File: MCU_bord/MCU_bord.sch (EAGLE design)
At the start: 1 part

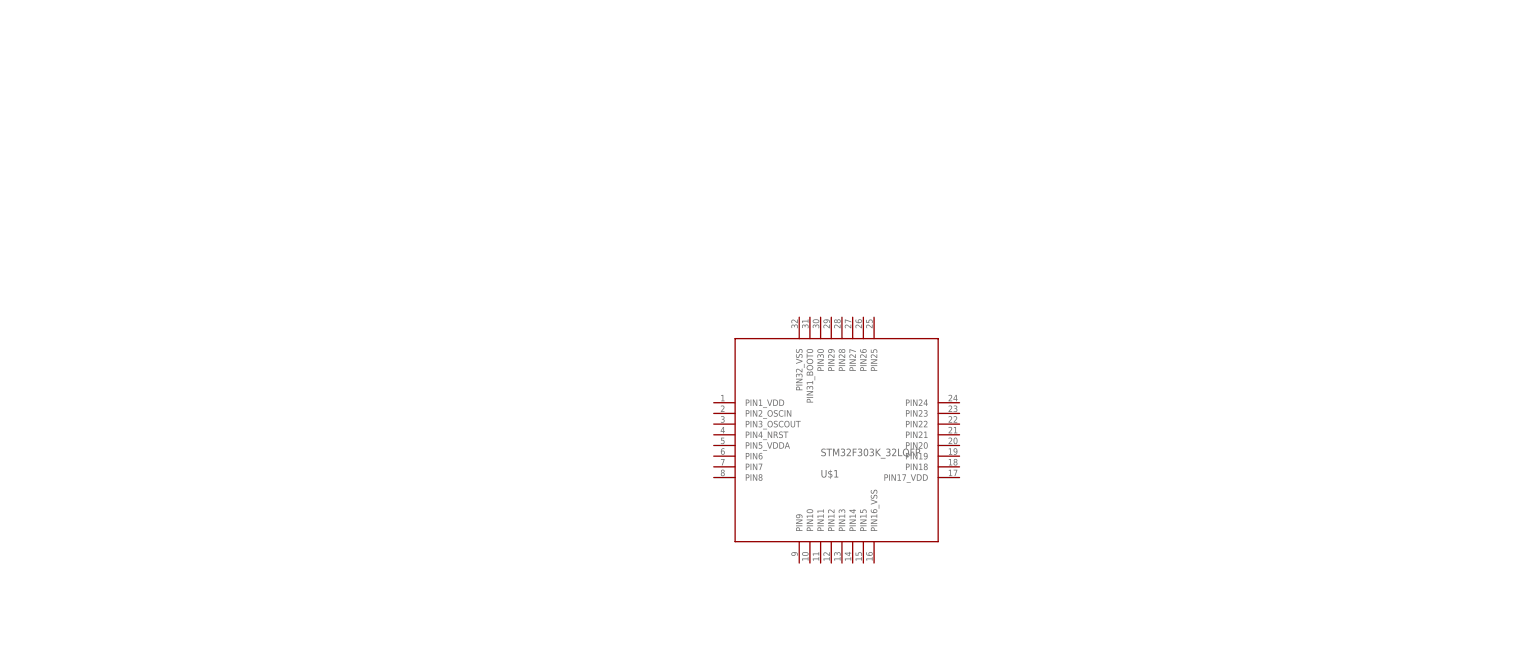
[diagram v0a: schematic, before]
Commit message: mcu側に着手
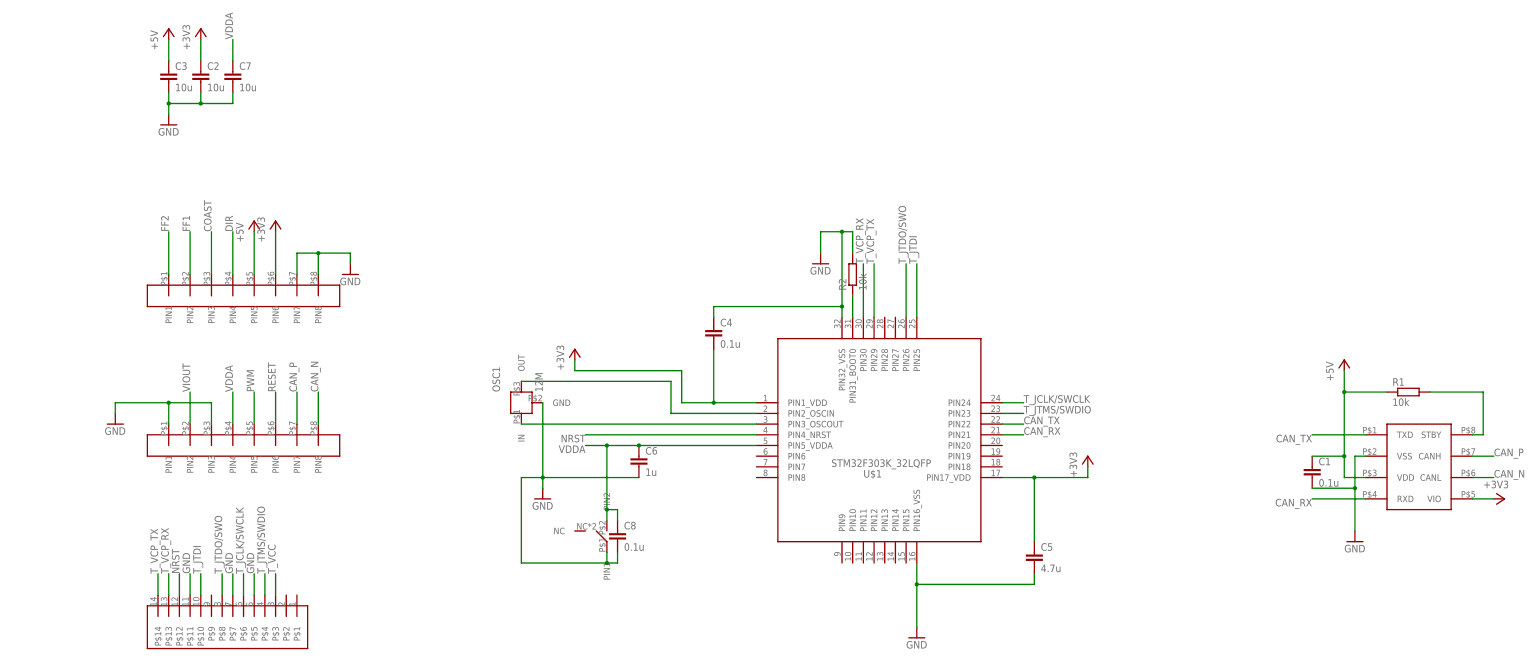
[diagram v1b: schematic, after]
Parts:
- added C1, C4, C8: 0.1u, rcl:C-EUC1608
- added C2, C3, C7: 10u, rcl:C-EUC1608
- added C5: 4.7u, rcl:C-EUC1608
- added C6: 1u, rcl:C-EUC1608
- added CON1, CON2: (no value), user_conector:JQ_S8P
- added IC1: (no value), user_ic:MCP2562MCP2561-SN
- added OSC1: 12M, user_osc:CSTN#
- added R1, R2: 10k, user_rcl:R_REG
- added U$2: TAKUTOSUITTI2, user_swich:TAKUTOSUITTI2
- added U$3: BOX14P, user_conector:BOX14P
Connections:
- new net +3V3: C2.1, C4.2, C5.1, CON1.PIN6, IC1.VIO, U$1.PIN17_VDD, U$1.PIN1_VDD
- new net +5V: C1.1, C3.1, CON1.PIN5, IC1.VDD, R1.1
- new net CAN_N: CON2.PIN8, IC1.CANL
- new net CAN_P: CON2.PIN7, IC1.CANH
- new net CAN_RX: IC1.RXD, U$1.PIN21
- new net CAN_TX: IC1.TXD, U$1.PIN22
- new net COAST: CON1.PIN3
- new net DIR: CON1.PIN4
- new net FF1: CON1.PIN2
- new net FF2: CON1.PIN1
- new net GND: C1.2, C2.2, C3.2, C4.1, C5.2, C6.2, C7.2, C8.2, CON1.PIN7, CON1.PIN8, CON2.PIN1, CON2.PIN3, IC1.VSS, OSC1.GND, R2.2, U$1.PIN16_VSS, U$1.PIN32_VSS, U$2.PIN1, U$3.P$11, U$3.P$5, U$3.P$7
- new net N$1: OSC1.IN, U$1.PIN3_OSCOUT
- new net N$2: OSC1.OUT, U$1.PIN2_OSCIN
- new net N$3: R2.1, U$1.PIN31_BOOT0
- new net N$7: IC1.STBY, R1.2
- new net NRST: U$1.PIN4_NRST, U$3.P$12
- new net PWM: CON2.PIN5
- new net RESET: CON2.PIN6
- new net T_JCLK/SWCLK: U$1.PIN24, U$3.P$6
- new net T_JTDI: U$1.PIN25, U$3.P$10
- new net T_JTDO/SWO: U$1.PIN26, U$3.P$8
- new net T_JTMS/SWDIO: U$1.PIN23, U$3.P$4
- new net T_VCC: U$3.P$3
- new net T_VCP_RX: U$1.PIN30, U$3.P$13
- new net T_VCP_TX: U$1.PIN29, U$3.P$14
- new net VDDA: C6.1, C7.1, C8.1, CON2.PIN4, U$1.PIN5_VDDA, U$2.PIN2
- new net VIOUT: CON2.PIN2
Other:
- moved on the sheet: U$1

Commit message: mcu側回路図多分完成。基板側に着手する予定
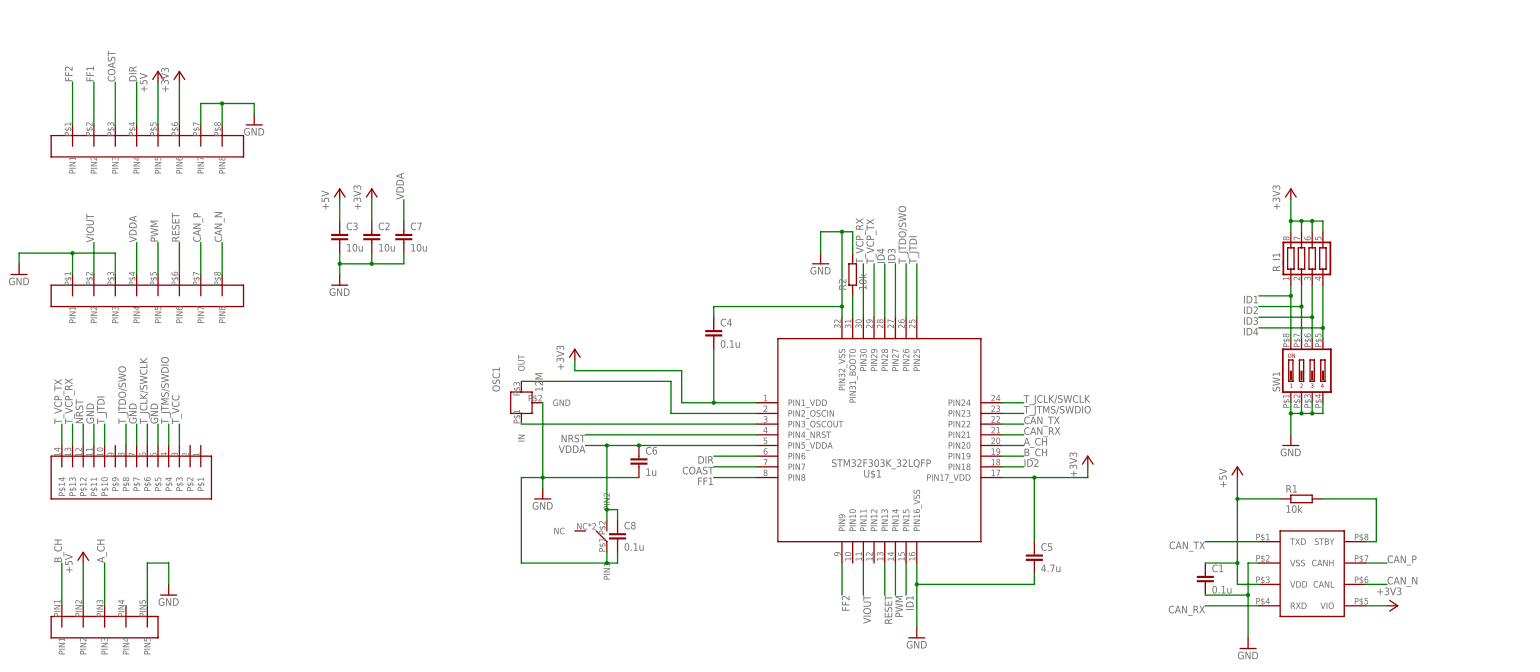
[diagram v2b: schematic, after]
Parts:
- added R_I1: (no value), user_rcl:R_SHUGOU2
- added SW1: (no value), user_swich:DIPSW4
- added U$4: ZH_5P, user_conector:ZH_5P
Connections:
- new net A_CH: U$1.PIN20, U$4.PIN3
- new net B_CH: U$1.PIN19, U$4.PIN1
- new net ID1: R_I1.1, SW1.8, U$1.PIN15
- new net ID2: R_I1.2, SW1.7, U$1.PIN18
- new net ID3: R_I1.3, SW1.6, U$1.PIN27
- new net ID4: R_I1.4, SW1.5, U$1.PIN28
- net +3V3: now also R_I1.5, R_I1.6, R_I1.7, R_I1.8
- net +5V: now also U$4.PIN2
- net COAST: now also U$1.PIN7
- net DIR: now also U$1.PIN6
- net FF1: now also U$1.PIN8
- net FF2: now also U$1.PIN9
- net GND: now also SW1.1, SW1.2, SW1.3, SW1.4, U$4.PIN5
- net PWM: now also U$1.PIN14
- net RESET: now also U$1.PIN13
- net VIOUT: now also U$1.PIN11
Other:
- moved on the sheet: C1, C2, C3, C7, R1

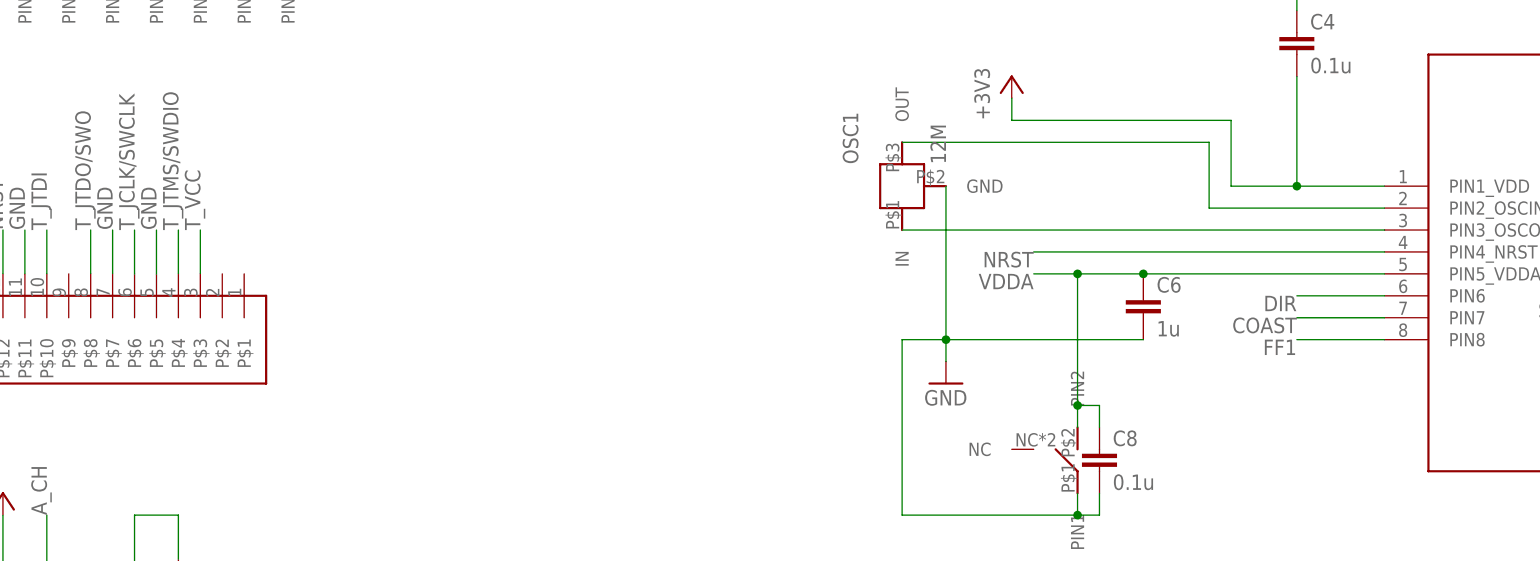
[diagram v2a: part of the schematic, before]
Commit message: MCU側完成。文字の位置とかの調整をやれば発注できる
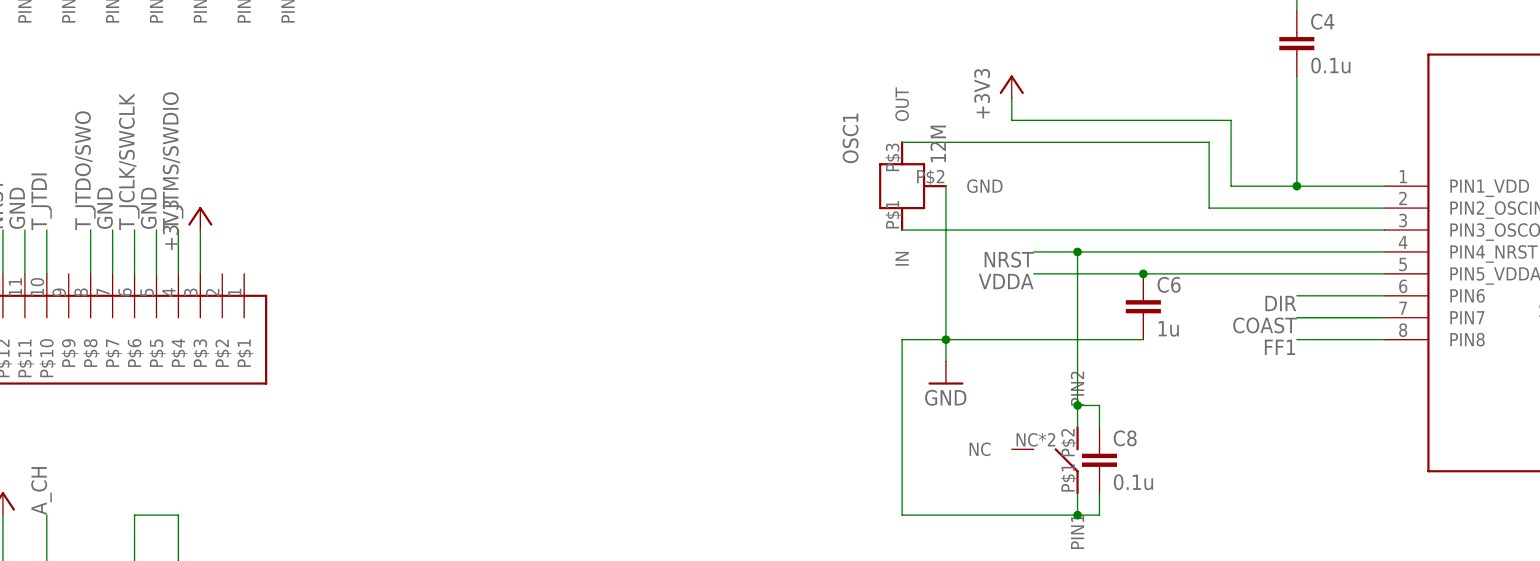
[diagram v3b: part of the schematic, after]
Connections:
- removed net T_VCC: U$3.P$3
- net +3V3: now also U$3.P$3
- net NRST: now also C8.1, U$2.PIN2
- net VDDA: no longer C8.1, U$2.PIN2
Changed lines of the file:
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@@
 <part name="GND9" library="supply1" library_urn="urn:adsk.eagle:library:371" deviceset="GND" device=""/>
 <part name="+3V6" library="supply1" library_urn="urn:adsk.eagle:library:371" deviceset="+3V3" device=""/>
+<part name="+3V7" library="supply1" library_urn="urn:adsk.eagle:library:371" deviceset="+3V3" device=""/>
 </parts>
 <sheets>
@@
 <attribute name="VALUE" x="177.8" y="106.68" size="1.778" layer="96" rot="R90"/>
 </instance>
+<instance part="+3V7" gate="G$1" x="-83.82" y="58.42" smashed="yes">
+<attribute name="VALUE" x="-86.36" y="53.34" size="1.778" layer="96" rot="R90"/>
+</instance>
 </instances>
 <busses>
@@
 <label x="12.7" y="50.8" size="1.778" layer="95" rot="R180"/>
 <pinref part="C6" gate="G$1" pin="1"/>
-<wire x1="25.4" y1="50.8" x2="17.78" y2="50.8" width="0.1524" layer="91"/>
+<wire x1="25.4" y1="50.8" x2="12.7" y2="50.8" width="0.1524" layer="91"/>
 <junction x="25.4" y="50.8"/>
-<pinref part="U$2" gate="G$1" pin="PIN2"/>
-<wire x1="17.78" y1="50.8" x2="12.7" y2="50.8" width="0.1524" layer="91"/>
-<wire x1="17.78" y1="33.02" x2="17.78" y2="35.56" width="0.1524" layer="91"/>
-<wire x1="17.78" y1="35.56" x2="20.32" y2="35.56" width="0.1524" layer="91"/>
-<pinref part="C8" gate="G$1" pin="1"/>
-<wire x1="20.32" y1="35.56" x2="20.32" y2="33.02" width="0.1524" layer="91"/>
-<wire x1="17.78" y1="35.56" x2="17.78" y2="50.8" width="0.1524" layer="91"/>
-<junction x="17.78" y="35.56"/>
-<junction x="17.78" y="50.8"/>
 </segment>
 <segment>
@@
 <junction x="185.42" y="104.14"/>
 </segment>
+<segment>
+<pinref part="U$3" gate="G$1" pin="P$3"/>
+<pinref part="+3V7" gate="G$1" pin="+3V3"/>
+<wire x1="-83.82" y1="50.8" x2="-83.82" y2="55.88" width="0.1524" layer="91"/>
+</segment>
 </net>
 <net name="N$7" class="0">
@@
 <segment>
 <pinref part="U$1" gate="G$1" pin="PIN4_NRST"/>
-<wire x1="53.34" y1="53.34" x2="12.7" y2="53.34" width="0.1524" layer="91"/>
+<wire x1="53.34" y1="53.34" x2="17.78" y2="53.34" width="0.1524" layer="91"/>
 <label x="12.7" y="53.34" size="1.778" layer="95" rot="R180"/>
+<pinref part="C8" gate="G$1" pin="1"/>
+<wire x1="17.78" y1="53.34" x2="12.7" y2="53.34" width="0.1524" layer="91"/>
+<wire x1="20.32" y1="35.56" x2="20.32" y2="33.02" width="0.1524" layer="91"/>
+<wire x1="17.78" y1="35.56" x2="20.32" y2="35.56" width="0.1524" layer="91"/>
+<pinref part="U$2" gate="G$1" pin="PIN2"/>
+<wire x1="17.78" y1="33.02" x2="17.78" y2="35.56" width="0.1524" layer="91"/>
+<wire x1="17.78" y1="35.56" x2="17.78" y2="53.34" width="0.1524" layer="91"/>
+<junction x="17.78" y="35.56"/>
+<junction x="17.78" y="53.34"/>
 </segment>
 <segment>
@@
 </segment>
 </net>
-<net name="T_VCC" class="0">
-<segment>
-<pinref part="U$3" gate="G$1" pin="P$3"/>
-<wire x1="-83.82" y1="50.8" x2="-83.82" y2="55.88" width="0.1524" layer="91"/>
-<label x="-83.82" y="55.88" size="1.778" layer="95" rot="R90"/>
-</segment>
-</net>

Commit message: TIMピンの選択ミスったのなおした
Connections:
- net A_CH: now also U$1.PIN8; no longer U$1.PIN20
- net B_CH: now also U$1.PIN7; no longer U$1.PIN19
- net COAST: now also U$1.PIN28; no longer U$1.PIN7
- net DIR: now also U$1.PIN27; no longer U$1.PIN6
- net FF1: now also U$1.PIN6; no longer U$1.PIN8
- net ID3: now also U$1.PIN19; no longer U$1.PIN27
- net ID4: now also U$1.PIN20; no longer U$1.PIN28
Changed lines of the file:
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@@
 </segment>
 <segment>
-<pinref part="U$1" gate="G$1" pin="PIN8"/>
-<wire x1="53.34" y1="43.18" x2="43.18" y2="43.18" width="0.1524" layer="91"/>
-<label x="43.18" y="43.18" size="1.778" layer="95" rot="R180"/>
+<pinref part="U$1" gate="G$1" pin="PIN6"/>
+<wire x1="53.34" y1="48.26" x2="43.18" y2="48.26" width="0.1524" layer="91"/>
+<label x="43.18" y="48.26" size="1.778" layer="95" rot="R180"/>
 </segment>
 </net>
@@
 </segment>
 <segment>
-<pinref part="U$1" gate="G$1" pin="PIN7"/>
-<wire x1="53.34" y1="45.72" x2="43.18" y2="45.72" width="0.1524" layer="91"/>
-<label x="43.18" y="45.72" size="1.778" layer="95" rot="R180"/>
+<pinref part="U$1" gate="G$1" pin="PIN28"/>
+<wire x1="83.82" y1="81.28" x2="83.82" y2="93.98" width="0.1524" layer="91"/>
+<label x="83.82" y="93.98" size="1.778" layer="95" rot="R90"/>
 </segment>
 </net>
@@
 </segment>
 <segment>
-<pinref part="U$1" gate="G$1" pin="PIN6"/>
-<wire x1="53.34" y1="48.26" x2="43.18" y2="48.26" width="0.1524" layer="91"/>
-<label x="43.18" y="48.26" size="1.778" layer="95" rot="R180"/>
+<pinref part="U$1" gate="G$1" pin="PIN27"/>
+<wire x1="86.36" y1="81.28" x2="86.36" y2="93.98" width="0.1524" layer="91"/>
+<label x="86.36" y="93.98" size="1.778" layer="95" rot="R90"/>
 </segment>
 </net>
@@
 </segment>
 <segment>
-<pinref part="U$1" gate="G$1" pin="PIN19"/>
-<wire x1="111.76" y1="48.26" x2="116.84" y2="48.26" width="0.1524" layer="91"/>
-<label x="116.84" y="48.26" size="1.778" layer="95"/>
+<pinref part="U$1" gate="G$1" pin="PIN7"/>
+<wire x1="53.34" y1="45.72" x2="43.18" y2="45.72" width="0.1524" layer="91"/>
+<label x="43.18" y="45.72" size="1.778" layer="95" rot="R180"/>
 </segment>
 </net>
@@
 </segment>
 <segment>
-<pinref part="U$1" gate="G$1" pin="PIN20"/>
-<wire x1="111.76" y1="50.8" x2="116.84" y2="50.8" width="0.1524" layer="91"/>
-<label x="116.84" y="50.8" size="1.778" layer="95"/>
+<pinref part="U$1" gate="G$1" pin="PIN8"/>
+<wire x1="53.34" y1="43.18" x2="43.18" y2="43.18" width="0.1524" layer="91"/>
+<label x="43.18" y="43.18" size="1.778" layer="95" rot="R180"/>
 </segment>
 </net>
@@
 <net name="ID3" class="0">
 <segment>
-<pinref part="U$1" gate="G$1" pin="PIN27"/>
-<wire x1="86.36" y1="81.28" x2="86.36" y2="93.98" width="0.1524" layer="91"/>
-<label x="86.36" y="93.98" size="1.778" layer="95" rot="R90"/>
-</segment>
-<segment>
 <pinref part="R_I1" gate="G$1" pin="3"/>
 <pinref part="SW1" gate="G$1" pin="6"/>
@@
 <label x="172.72" y="81.28" size="1.778" layer="95" rot="R180"/>
 </segment>
+<segment>
+<pinref part="U$1" gate="G$1" pin="PIN19"/>
+<wire x1="111.76" y1="48.26" x2="116.84" y2="48.26" width="0.1524" layer="91"/>
+<label x="116.84" y="48.26" size="1.778" layer="95"/>
+</segment>
 </net>
 <net name="ID4" class="0">
-<segment>
-<pinref part="U$1" gate="G$1" pin="PIN28"/>
-<wire x1="83.82" y1="81.28" x2="83.82" y2="93.98" width="0.1524" layer="91"/>
-<label x="83.82" y="93.98" size="1.778" layer="95" rot="R90"/>
-</segment>
 <segment>
 <pinref part="R_I1" gate="G$1" pin="4"/>
@@
 <label x="172.72" y="78.74" size="1.778" layer="95" rot="R180"/>
 </segment>
-</net>
+<segment>
+<pinref part="U$1" gate="G$1" pin="PIN20"/>
+<wire x1="111.76" y1="50.8" x2="116.84" y2="50.8" width="0.1524" layer="91"/>
+<label x="116.84" y="50.8" size="1.778" layer="95"/>
+</segment>
+</net>

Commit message: ミス直し
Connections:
- net A_CH: now also U$1.PIN7; no longer U$1.PIN8
- net B_CH: now also U$1.PIN6; no longer U$1.PIN7
- net FF1: now also U$1.PIN8; no longer U$1.PIN6
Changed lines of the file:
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@@
 </segment>
 <segment>
-<pinref part="U$1" gate="G$1" pin="PIN6"/>
-<wire x1="53.34" y1="48.26" x2="43.18" y2="48.26" width="0.1524" layer="91"/>
-<label x="43.18" y="48.26" size="1.778" layer="95" rot="R180"/>
+<pinref part="U$1" gate="G$1" pin="PIN8"/>
+<wire x1="53.34" y1="43.18" x2="40.64" y2="43.18" width="0.1524" layer="91"/>
+<label x="40.64" y="43.18" size="1.778" layer="95" rot="R180"/>
 </segment>
 </net>
@@
 </segment>
 <segment>
-<pinref part="U$1" gate="G$1" pin="PIN7"/>
-<wire x1="53.34" y1="45.72" x2="43.18" y2="45.72" width="0.1524" layer="91"/>
-<label x="43.18" y="45.72" size="1.778" layer="95" rot="R180"/>
+<pinref part="U$1" gate="G$1" pin="PIN6"/>
+<wire x1="53.34" y1="48.26" x2="40.64" y2="48.26" width="0.1524" layer="91"/>
+<label x="40.64" y="48.26" size="1.778" layer="95" rot="R180"/>
 </segment>
 </net>
@@
 </segment>
 <segment>
-<pinref part="U$1" gate="G$1" pin="PIN8"/>
-<wire x1="53.34" y1="43.18" x2="43.18" y2="43.18" width="0.1524" layer="91"/>
-<label x="43.18" y="43.18" size="1.778" layer="95" rot="R180"/>
-</segment>
-</net>
+<pinref part="U$1" gate="G$1" pin="PIN7"/>
+<wire x1="53.34" y1="45.72" x2="40.64" y2="45.72" width="0.1524" layer="91"/>
+<label x="40.64" y="45.72" size="1.778" layer="95" rot="R180"/>
+</segment>
+</net>

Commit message: 基板エラー修正
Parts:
- removed R1: 10k, user_rcl:R_REG
- removed U$4: ZH_5P, user_conector:ZH_5P
- added CON3: (no value), user_conector:XH_5P
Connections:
- removed net N$7: IC1.STBY, R1.2
- net +3V3: now also SW1.5, SW1.6, SW1.7, SW1.8; no longer R_I1.5, R_I1.6, R_I1.7, R_I1.8
- net +5V: now also CON3.PIN2; no longer R1.1, U$4.PIN2
- net A_CH: now also CON3.PIN3; no longer U$4.PIN3
- net B_CH: now also CON3.PIN1; no longer U$4.PIN1
- net GND: now also CON3.PIN5, IC1.STBY, R_I1.1, R_I1.2, R_I1.3, R_I1.4; no longer SW1.1, SW1.2, SW1.3, SW1.4, U$4.PIN5
- net ID1: now also R_I1.8, SW1.1; no longer R_I1.1, SW1.8
- net ID2: now also R_I1.7, SW1.2; no longer R_I1.2, SW1.7
- net ID3: now also R_I1.6, SW1.3; no longer R_I1.3, SW1.6
- net ID4: now also R_I1.5, SW1.4; no longer R_I1.4, SW1.5
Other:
- moved on the sheet: R_I1, SW1
